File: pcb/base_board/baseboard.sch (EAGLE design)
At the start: 38 parts, among them IC1 LD117AS33TR, SW1 324_SW, SW2 324_SW, SW20 324_SW, SW3 324_SW, SW4 324_SW, U5 CH340C

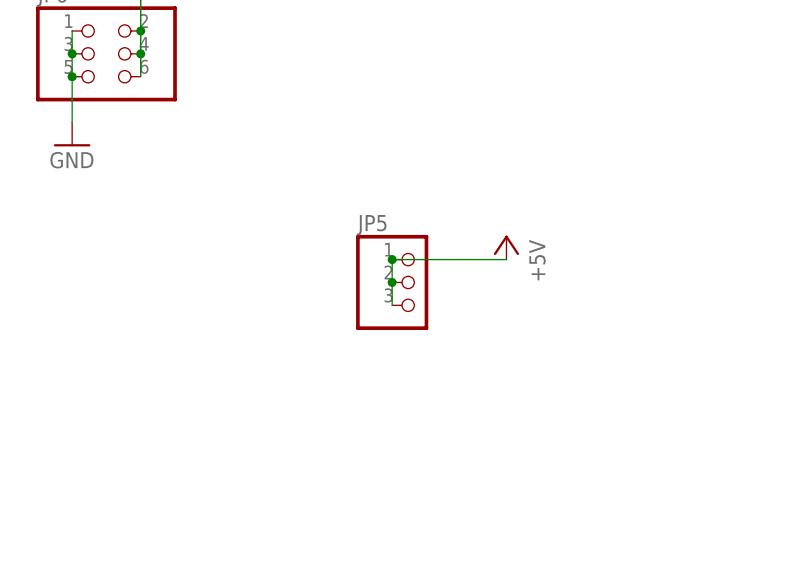
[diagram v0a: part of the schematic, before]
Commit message: updated PCB for second prototype run
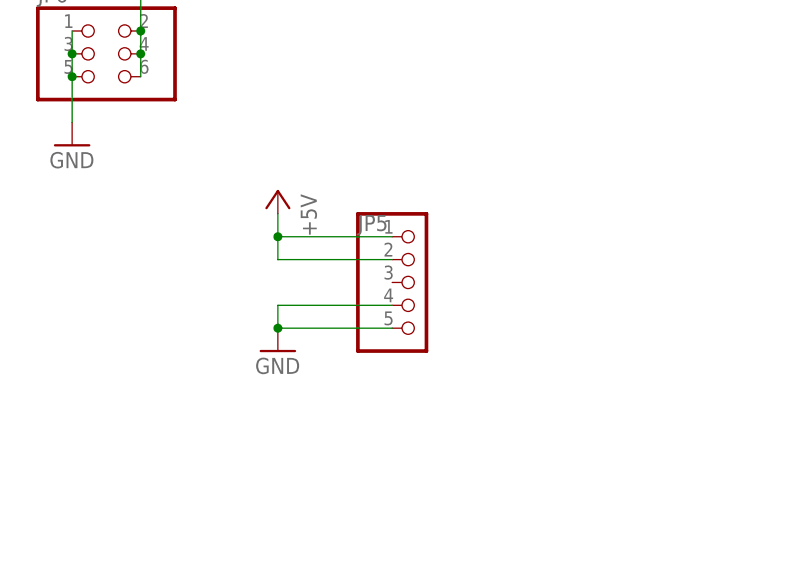
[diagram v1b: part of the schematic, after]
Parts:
- JP5: device pinhead:PINHD-1X3 -> pinhead:PINHD-1X5
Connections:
- net +5V: no longer JP5.3
- net GND: now also JP5.4, JP5.5
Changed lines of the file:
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@@
 <part name="+3V1" library="supply1" library_urn="urn:adsk.eagle:library:371" deviceset="+3V3" device=""/>
 <part name="+3V4" library="supply1" library_urn="urn:adsk.eagle:library:371" deviceset="+3V3" device=""/>
-<part name="JP5" library="pinhead" library_urn="urn:adsk.eagle:library:325" deviceset="PINHD-1X3" device="" package3d_urn="urn:adsk.eagle:package:22458/2"/>
+<part name="JP5" library="pinhead" library_urn="urn:adsk.eagle:library:325" deviceset="PINHD-1X5" device="" package3d_urn="urn:adsk.eagle:package:22469/2"/>
 <part name="P+3" library="supply1" library_urn="urn:adsk.eagle:library:371" deviceset="+5V" device=""/>
 <part name="+3V6" library="supply1" library_urn="urn:adsk.eagle:library:371" deviceset="+3V3" device=""/>
@@
 <part name="+3V15" library="supply1" library_urn="urn:adsk.eagle:library:371" deviceset="+3V3" device=""/>
 <part name="JP6" library="pinhead" library_urn="urn:adsk.eagle:library:325" deviceset="PINHD-2X3" device="" package3d_urn="urn:adsk.eagle:package:22462/2"/>
+<part name="GND13" library="supply1" library_urn="urn:adsk.eagle:library:371" deviceset="GND" device=""/>
 </parts>
 <sheets>
@@
 <attribute name="VALUE" x="796.29" y="63.5" size="1.778" layer="96"/>
 </instance>
-<instance part="P+3" gate="1" x="812.8" y="76.2" smashed="yes" rot="MR0">
-<attribute name="VALUE" x="815.34" y="71.12" size="1.778" layer="96" rot="MR90"/>
+<instance part="P+3" gate="1" x="787.4" y="81.28" smashed="yes" rot="MR0">
+<attribute name="VALUE" x="789.94" y="76.2" size="1.778" layer="96" rot="MR90"/>
 </instance>
 <instance part="+3V6" gate="G$1" x="772.16" y="111.76" smashed="yes">
@@
 <attribute name="NAME" x="760.73" y="102.235" size="1.778" layer="95"/>
 <attribute name="VALUE" x="760.73" y="88.9" size="1.778" layer="96"/>
+</instance>
+<instance part="GND13" gate="1" x="787.4" y="63.5" smashed="yes">
+<attribute name="VALUE" x="784.86" y="60.96" size="1.778" layer="96"/>
 </instance>
 </instances>
@@
 <junction x="764.54" y="93.98"/>
 </segment>
+<segment>
+<pinref part="JP5" gate="A" pin="5"/>
+<pinref part="GND13" gate="1" pin="GND"/>
+<wire x1="800.1" y1="66.04" x2="787.4" y2="66.04" width="0.1524" layer="91"/>
+<pinref part="JP5" gate="A" pin="4"/>
+<wire x1="800.1" y1="68.58" x2="787.4" y2="68.58" width="0.1524" layer="91"/>
+<wire x1="787.4" y1="68.58" x2="787.4" y2="66.04" width="0.1524" layer="91"/>
+<junction x="787.4" y="66.04"/>
+</segment>
 </net>
 <net name="+5V" class="0">
@@
 <segment>
 <pinref part="P+3" gate="1" pin="+5V"/>
+<wire x1="787.4" y1="78.74" x2="787.4" y2="76.2" width="0.1524" layer="91"/>
+<pinref part="JP5" gate="A" pin="2"/>
+<wire x1="787.4" y1="76.2" x2="787.4" y2="73.66" width="0.1524" layer="91"/>
+<wire x1="787.4" y1="73.66" x2="800.1" y2="73.66" width="0.1524" layer="91"/>
 <pinref part="JP5" gate="A" pin="1"/>
-<wire x1="812.8" y1="73.66" x2="800.1" y2="73.66" width="0.1524" layer="91"/>
-<pinref part="JP5" gate="A" pin="2"/>
-<wire x1="800.1" y1="73.66" x2="800.1" y2="71.12" width="0.1524" layer="91"/>
-<junction x="800.1" y="73.66"/>
-<pinref part="JP5" gate="A" pin="3"/>
-<wire x1="800.1" y1="71.12" x2="800.1" y2="68.58" width="0.1524" layer="91"/>
-<junction x="800.1" y="71.12"/>
+<wire x1="800.1" y1="76.2" x2="787.4" y2="76.2" width="0.1524" layer="91"/>
+<junction x="787.4" y="76.2"/>
 </segment>
 </net>

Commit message: added gerber file
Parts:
- removed C25: 1uF, clock:CAP0805
- added JP3: (no value), adafruit_changed:PINHD-1X1
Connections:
- net +3V3: no longer C25.2
- net GND: no longer C25.1
- net N$32: now also JP3.1
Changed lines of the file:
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@@
 <part name="GND22" library="supply1" library_urn="urn:adsk.eagle:library:371" deviceset="GND" device=""/>
 <part name="C24" library="clock" deviceset="CAP" device="0805" value="100nF"/>
-<part name="C25" library="clock" deviceset="CAP" device="0805" value="1uF"/>
 <part name="P+4" library="supply1" library_urn="urn:adsk.eagle:library:371" deviceset="+5V" device=""/>
 <part name="GND7" library="supply1" library_urn="urn:adsk.eagle:library:371" deviceset="GND" device=""/>
@@
 <part name="JP6" library="pinhead" library_urn="urn:adsk.eagle:library:325" deviceset="PINHD-2X3" device="" package3d_urn="urn:adsk.eagle:package:22462/2"/>
 <part name="GND13" library="supply1" library_urn="urn:adsk.eagle:library:371" deviceset="GND" device=""/>
+<part name="JP3" library="adafruit_changed" deviceset="PINHD-1X1" device=""/>
 </parts>
 <sheets>
@@
 <attribute name="VALUE" x="928.116" y="-30.861" size="1.778" layer="96" rot="R180"/>
 </instance>
-<instance part="C25" gate="G$1" x="919.48" y="-33.02" smashed="yes" rot="R180">
-<attribute name="NAME" x="917.956" y="-35.941" size="1.778" layer="95" rot="R180"/>
-<attribute name="VALUE" x="917.956" y="-30.861" size="1.778" layer="96" rot="R180"/>
-</instance>
 <instance part="P+4" gate="1" x="665.48" y="101.6" smashed="yes" rot="MR0">
 <attribute name="VALUE" x="668.02" y="96.52" size="1.778" layer="96" rot="MR90"/>
@@
 <instance part="GND13" gate="1" x="787.4" y="63.5" smashed="yes">
 <attribute name="VALUE" x="784.86" y="60.96" size="1.778" layer="96"/>
+</instance>
+<instance part="JP3" gate="G$1" x="756.92" y="0" smashed="yes">
+<attribute name="NAME" x="750.57" y="3.175" size="1.778" layer="95"/>
+<attribute name="VALUE" x="750.57" y="-5.08" size="1.778" layer="96"/>
 </instance>
 </instances>
@@
 <pinref part="GND22" gate="1" pin="GND"/>
 <wire x1="947.42" y1="-38.1" x2="929.64" y2="-38.1" width="0.1524" layer="91"/>
-<wire x1="929.64" y1="-38.1" x2="919.48" y2="-38.1" width="0.1524" layer="91"/>
-<wire x1="919.48" y1="-38.1" x2="911.86" y2="-38.1" width="0.1524" layer="91"/>
 <junction x="947.42" y="-38.1"/>
 <pinref part="C5" gate="G$1" pin="1"/>
-<wire x1="947.42" y1="-38.1" x2="977.9" y2="-38.1" width="0.1524" layer="91"/>
 <pinref part="C24" gate="G$1" pin="1"/>
-<junction x="929.64" y="-38.1"/>
-<pinref part="C25" gate="G$1" pin="1"/>
-<junction x="919.48" y="-38.1"/>
 </segment>
 <segment>
@@
 <wire x1="947.42" y1="-25.4" x2="947.42" y2="-30.48" width="0.1524" layer="91"/>
 <wire x1="947.42" y1="-30.48" x2="929.64" y2="-30.48" width="0.1524" layer="91"/>
-<wire x1="929.64" y1="-30.48" x2="919.48" y2="-30.48" width="0.1524" layer="91"/>
-<wire x1="919.48" y1="-30.48" x2="911.86" y2="-30.48" width="0.1524" layer="91"/>
 <junction x="947.42" y="-30.48"/>
 <pinref part="C5" gate="G$1" pin="2"/>
-<wire x1="947.42" y1="-30.48" x2="977.9" y2="-30.48" width="0.1524" layer="91"/>
 <pinref part="C24" gate="G$1" pin="2"/>
-<junction x="929.64" y="-30.48"/>
-<pinref part="C25" gate="G$1" pin="2"/>
-<junction x="919.48" y="-30.48"/>
 </segment>
 <segment>
@@
 <pinref part="R5" gate="G$1" pin="1"/>
 <junction x="721.36" y="0"/>
-</segment>
-</net>
+<pinref part="JP3" gate="G$1" pin="1"/>
+<wire x1="741.68" y1="0" x2="754.38" y2="0" width="0.1524" layer="91"/>
+<junction x="741.68" y="0"/>
+</segment>
+</net>

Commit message: updated component values
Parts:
- removed JP1, JP2: (no value), adafruit_changed:PINHD-2X20-BIG
- added P2, P3: (no value), adafruit_changed:PINHD-2X20-BIG
- C29: value 10uF -> 2.2uF
- R2, R3, R5, R6: value 390K -> 5.1K
- R8: value 12K -> 5.1K
- renumbered PCB1 to P1
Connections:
- net +3V3: now also P2.1, P2.17, P3.1, P3.17; no longer JP1.1, JP1.17, JP2.1, JP2.17
- net +5V: now also P2.2, P2.4, P3.2, P3.4; no longer JP1.2, JP1.4, JP2.2, JP2.4
- net ENTER_BUTTON: now also P2.15, P3.15; no longer JP1.15, JP2.15
- net GND: now also P2.14, P2.20, P2.25, P2.30, P2.34, P2.39, P2.6, P2.9, P3.14, P3.20, P3.25, P3.30, P3.34, P3.39, P3.6, P3.9; no longer JP1.14, JP1.20, JP1.25, JP1.30, JP1.34, JP1.39, JP1.6, JP1.9, JP2.14, JP2.20, JP2.25, JP2.30, JP2.34, JP2.39, JP2.6, JP2.9
- net MINUS_BUTTON: now also P2.35, P3.35; no longer JP1.35, JP2.35
- net N$12: now also P2.19, P3.19; no longer JP1.19, JP2.19
- net N$13: now also P2.21, P3.21; no longer JP1.21, JP2.21
- net N$14: now also P2.23, P3.23; no longer JP1.23, JP2.23
- net N$15: now also P2.27, P3.27; no longer JP1.27, JP2.27
- net N$16: now also P2.29, P3.29; no longer JP1.29, JP2.29
- net N$19: now also P2.33, P3.33; no longer JP1.33, JP2.33
- net N$21: now also P2.37, P3.37; no longer JP1.37, JP2.37
- net N$22: now also P2.12, P3.12; no longer JP1.12, JP2.12
- net N$23: now also P2.16, P3.16; no longer JP1.16, JP2.16
- net N$24: now also P2.18, P3.18; no longer JP1.18, JP2.18
- net N$25: now also P2.22, P3.22; no longer JP1.22, JP2.22
- net N$26: now also P2.24, P3.24; no longer JP1.24, JP2.24
- net N$27: now also P2.26, P3.26; no longer JP1.26, JP2.26
- net N$28: now also P2.28, P3.28; no longer JP1.28, JP2.28
- net N$29: now also P2.32, P3.32; no longer JP1.32, JP2.32
- net N$30: now also P2.36, P3.36; no longer JP1.36, JP2.36
- net N$31: now also P2.38, P3.38; no longer JP1.38, JP2.38
- net N$32: now also P2.40, P3.40; no longer JP1.40, JP2.40
- net N$43: now also P2.31, P3.31; no longer JP1.31, JP2.31
- net N$5: now also P2.3, P3.3; no longer JP1.3, JP2.3
- net N$6: now also P2.5, P3.5; no longer JP1.5, JP2.5
- net N$8: now also P2.7, P3.7; no longer JP1.7, JP2.7
- net N$9: now also P2.11, P3.11; no longer JP1.11, JP2.11
- net PLUS_BUTTON: now also P2.13, P3.13; no longer JP1.13, JP2.13
- net RPI_RX: now also P2.10, P3.10; no longer JP1.10, JP2.10
- net RPI_TX: now also P2.8, P3.8; no longer JP1.8, JP2.8
